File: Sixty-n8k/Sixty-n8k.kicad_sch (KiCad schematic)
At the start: 65 parts, among them J1 USB4085-GF-A_REVB, J2 SD_CARD_PORT, J3 Conn_02x32_Odd_Even, J4 Conn_01x02, SW1 RESET, SW2 DEBUG, U1 74LS05, U10 74HC164, U11 74LS393, U13 74LS148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

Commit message: Starting to hand route. want to just layout and see what autorouter does though...
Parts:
- D1: value LED_ALT -> POWER; symbol n8-bit-special-rescue:LED_ALT-Device -> Device:LED
- D2: value LED_ALT -> HALT; symbol n8-bit-special-rescue:LED_ALT-Device -> Device:LED
- D3: value LED_ALT -> RX; symbol n8-bit-special-rescue:LED_ALT-Device -> Device:LED
- D4: value LED_ALT -> TX; symbol n8-bit-special-rescue:LED_ALT-Device -> Device:LED
- J2: footprint Connector_PinHeader_2.54mm:PinHeader_2x08_P2.54mm_Vertical -> Connector_PinSocket_2.54mm:PinSocket_2x08_P2.54mm_Vertical
- J4: footprint Connector_PinSocket_2.54mm:PinSocket_1x02_P2.54mm_Vertical -> Connector_PinHeader_2.54mm:PinHeader_1x02_P2.54mm_Vertical
- U3: value AM29F040B-70J -> ODD_ROM
- U4: value AS6C4008-55PCN -> ODD_RAM
- U7: value AS6C4008-55PCN -> EVEN_RAM
- U8: value AM29F040B-70J -> EVEN_ROM
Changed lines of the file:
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@@
       (effects (font (size 1.27 1.27)) (justify left))
     )
-    (property "Value" "AS6C4008-55PCN" (at 342.3159 30.099 0)
+    (property "Value" "ODD_RAM" (at 342.3159 30.099 0)
       (effects (font (size 1.27 1.27)) (justify left))
     )
@@
     )
   )
-  (symbol (lib_id "n8-bit-special-rescue:LED_ALT-Device") (at 558.8 300.99 90) (unit 1)
+  (symbol (lib_id "Device:LED") (at 558.8 300.99 90) (unit 1)
     (in_bom yes) (on_board yes) (dnp no)
     (property "Reference" "D4" (at 553.2882 301.1678 0)
       (effects (font (size 1.27 1.27)))
     )
-    (property "Value" "LED_ALT" (at 555.5996 301.1678 0)
+    (property "Value" "TX" (at 555.5996 301.1678 0)
       (effects (font (size 1.27 1.27)))
     )
@@
       (effects (font (size 1.27 1.27)))
     )
-    (property "Footprint" "Connector_PinHeader_2.54mm:PinHeader_2x08_P2.54mm_Vertical" (at 530.86 207.01 0)
+    (property "Footprint" "Connector_PinSocket_2.54mm:PinSocket_2x08_P2.54mm_Vertical" (at 530.86 207.01 0)
       (effects (font (size 1.27 1.27)) hide)
     )
@@
     )
   )
-  (symbol (lib_id "n8-bit-special-rescue:LED_ALT-Device") (at 548.64 300.99 90) (unit 1)
+  (symbol (lib_id "Device:LED") (at 548.64 300.99 90) (unit 1)
     (in_bom yes) (on_board yes) (dnp no)
     (property "Reference" "D3" (at 543.1282 301.1678 0)
       (effects (font (size 1.27 1.27)))
     )
-    (property "Value" "LED_ALT" (at 545.4396 301.1678 0)
+    (property "Value" "RX" (at 545.4396 301.1678 0)
       (effects (font (size 1.27 1.27)))
     )
@@
     )
   )
-  (symbol (lib_id "n8-bit-special-rescue:LED_ALT-Device") (at 118.11 91.44 0) (unit 1)
+  (symbol (lib_id "Device:LED") (at 118.11 91.44 0) (unit 1)
     (in_bom yes) (on_board yes) (dnp no)
     (property "Reference" "D2" (at 117.9322 85.9282 0)
       (effects (font (size 1.27 1.27)))
     )
-    (property "Value" "LED_ALT" (at 117.9322 88.2396 0)
+    (property "Value" "HALT" (at 117.9322 88.2396 0)
       (effects (font (size 1.27 1.27)))
     )
@@
       (effects (font (size 1.27 1.27)) (justify left))
     )
-    (property "Value" "AM29F040B-70J" (at 433.7559 96.774 0)
+    (property "Value" "EVEN_ROM" (at 433.7559 96.774 0)
       (effects (font (size 1.27 1.27)) (justify left))
     )
@@
       (effects (font (size 1.27 1.27)) (justify left))
     )
-    (property "Value" "AM29F040B-70J" (at 433.7559 30.734 0)
+    (property "Value" "ODD_ROM" (at 433.7559 30.734 0)
       (effects (font (size 1.27 1.27)) (justify left))
     )
@@
     )
   )
-  (symbol (lib_id "n8-bit-special-rescue:LED_ALT-Device") (at 118.11 71.12 0) (unit 1)
+  (symbol (lib_id "Device:LED") (at 118.11 71.12 0) (unit 1)
     (in_bom yes) (on_board yes) (dnp no)
     (property "Reference" "D1" (at 117.9322 65.6082 0)
       (effects (font (size 1.27 1.27)))
     )
-    (property "Value" "LED_ALT" (at 117.9322 67.9196 0)
+    (property "Value" "POWER" (at 117.9322 67.9196 0)
       (effects (font (size 1.27 1.27)))
     )
@@
       (effects (font (size 1.27 1.27)) (justify left))
     )
-    (property "Footprint" "Connector_PinSocket_2.54mm:PinSocket_1x02_P2.54mm_Vertical" (at 314.325 216.535 0)
+    (property "Footprint" "Connector_PinHeader_2.54mm:PinHeader_1x02_P2.54mm_Vertical" (at 314.325 216.535 0)
       (effects (font (size 1.27 1.27)) hide)
     )
@@
       (effects (font (size 1.27 1.27)) (justify left))
     )
-    (property "Value" "AS6C4008-55PCN" (at 342.3159 96.139 0)
+    (property "Value" "EVEN_RAM" (at 342.3159 96.139 0)
       (effects (font (size 1.27 1.27)) (justify left))
     )

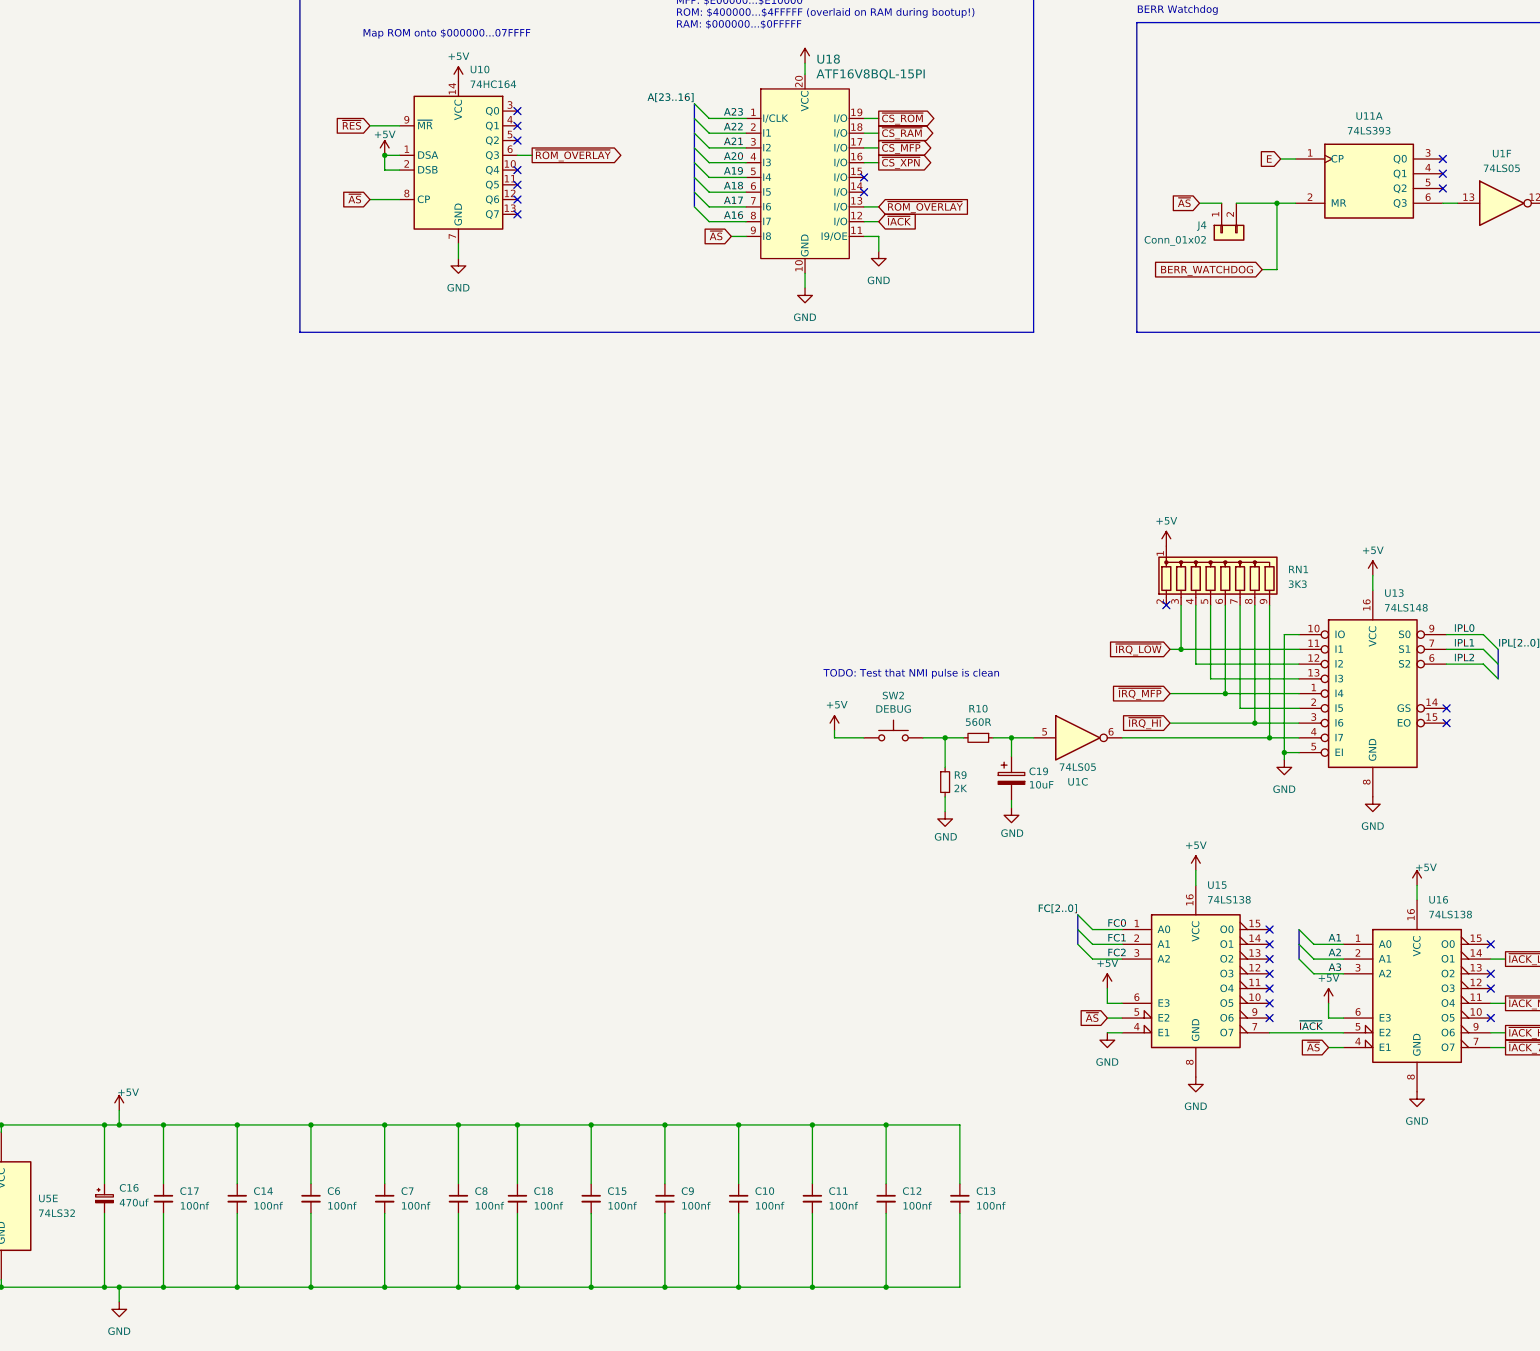
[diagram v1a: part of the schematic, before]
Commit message: new layout, start of hand routing but very complex
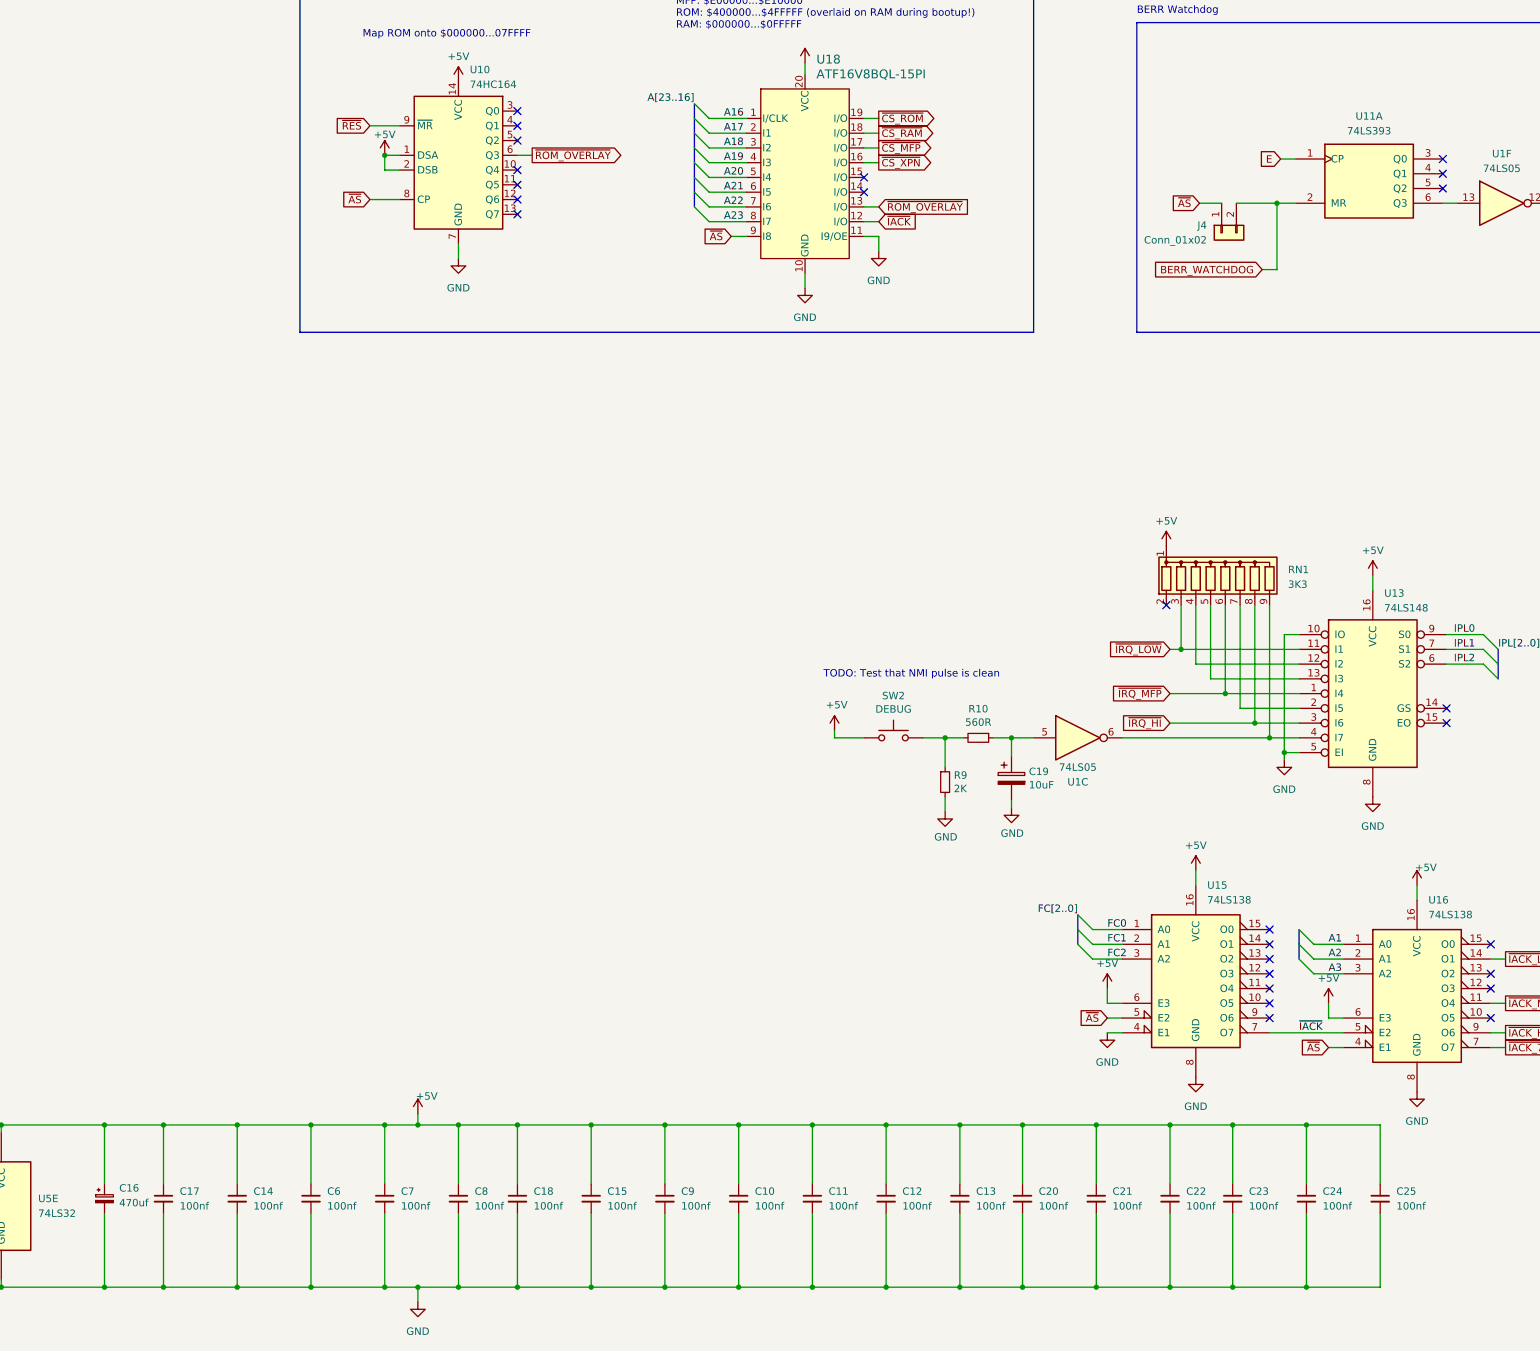
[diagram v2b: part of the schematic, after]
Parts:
- added C20, C21, C22, C23, C24, C25: 100nf, Capacitor_THT:C_Disc_D5.0mm_W2.5mm_P2.50mm, symbol Device:C_Small
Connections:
- net +5V: now also C20.1, C21.1, C22.1, C23.1, C24.1, C25.1
- net A16: now also U18.1 (I/CLK); no longer U18.8 (I7)
- net A17: now also U18.2 (I1); no longer U18.7 (I6)
- net A18: now also U18.3 (I2); no longer U18.6 (I5)
- net A19: now also U18.4 (I3); no longer U18.5 (I4)
- net A20: now also U18.5 (I4); no longer U18.4 (I3)
- net A21: now also U18.6 (I5); no longer U18.3 (I2)
- net A22: now also U18.7 (I6); no longer U18.2 (I1)
- net A23: now also U18.8 (I7); no longer U18.1 (I/CLK)
- net GND: now also C20.2, C21.2, C22.2, C23.2, C24.2, C25.2

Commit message: Autoroute success (don't judge me)
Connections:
- net A1: now also J3.31 (Pin_31); no longer J3.5 (Pin_5)
- net A10: now also J3.49 (Pin_49); no longer J3.23 (Pin_23)
- net A11: now also J3.51 (Pin_51); no longer J3.25 (Pin_25)
- net A12: now also J3.53 (Pin_53); no longer J3.27 (Pin_27)
- net A13: now also J3.55 (Pin_55); no longer J3.29 (Pin_29)
- net A14: now also J3.57 (Pin_57); no longer J3.31 (Pin_31)
- net A15: now also J3.59 (Pin_59); no longer J3.33 (Pin_33)
- net A2: now also J3.33 (Pin_33); no longer J3.7 (Pin_7)
- net A3: now also J3.35 (Pin_35); no longer J3.9 (Pin_9)
- net A4: now also J3.37 (Pin_37); no longer J3.11 (Pin_11)
- net A5: now also J3.39 (Pin_39); no longer J3.13 (Pin_13)
- net A6: now also J3.41 (Pin_41); no longer J3.15 (Pin_15)
- net A7: now also J3.43 (Pin_43); no longer J3.17 (Pin_17)
- net A8: now also J3.45 (Pin_45); no longer J3.19 (Pin_19)
- net A9: now also J3.47 (Pin_47); no longer J3.21 (Pin_21)
- net CLK_{CPU}: now also J3.29 (Pin_29); no longer J3.59 (Pin_59)
- net CLK_{HALF}: now also J3.18 (Pin_18); no longer J3.60 (Pin_60)
- net D0: now also J3.60 (Pin_60); no longer J3.6 (Pin_6)
- net D1: now also J3.58 (Pin_58); no longer J3.8 (Pin_8)
- net D10: now also J3.40 (Pin_40); no longer J3.26 (Pin_26)
- net D11: now also J3.38 (Pin_38); no longer J3.28 (Pin_28)
- net D12: now also J3.36 (Pin_36); no longer J3.30 (Pin_30)
- net D13: now also J3.34 (Pin_34); no longer J3.32 (Pin_32)
- net D14: now also J3.32 (Pin_32); no longer J3.34 (Pin_34)
- net D15: now also J3.30 (Pin_30); no longer J3.36 (Pin_36)
- net D2: now also J3.56 (Pin_56); no longer J3.10 (Pin_10)
- net D3: now also J3.54 (Pin_54); no longer J3.12 (Pin_12)
- net D4: now also J3.52 (Pin_52); no longer J3.14 (Pin_14)
- net D5: now also J3.50 (Pin_50); no longer J3.16 (Pin_16)
- net D6: now also J3.48 (Pin_48); no longer J3.18 (Pin_18)
- net D7: now also J3.46 (Pin_46); no longer J3.20 (Pin_20)
- net D8: now also J3.44 (Pin_44); no longer J3.22 (Pin_22)
- net D9: now also J3.42 (Pin_42); no longer J3.24 (Pin_24)
- net E: now also J3.21 (Pin_21); no longer J3.51 (Pin_51)
- net R~{W}: now also J3.9 (Pin_9); no longer J3.39 (Pin_39)
- net ~{AS}: now also J3.11 (Pin_11); no longer J3.41 (Pin_41)
- net ~{BERR}: now also J3.12 (Pin_12); no longer J3.54 (Pin_54)
- net ~{BGACK}: now also J3.28 (Pin_28), RN3.3 (R2); no longer J3.46 (Pin_46), RN2.9 (R8)
- net ~{BG}: now also J3.8 (Pin_8); no longer J3.50 (Pin_50)
- net ~{BR}: now also J3.10 (Pin_10), RN3.2 (R1); no longer J3.52 (Pin_52), RN2.8 (R7)
- net ~{CS_XPN}: now also J3.15 (Pin_15); no longer J3.45 (Pin_45)
- net ~{DTACK_MFP}: now also RN2.8 (R7); no longer RN3.2 (R1)
- net ~{DTACK_XPN}: now also J3.13 (Pin_13), RN2.9 (R8); no longer J3.43 (Pin_43), RN3.3 (R2)
- net ~{IACK_HI}: now also J3.26 (Pin_26); no longer J3.44 (Pin_44)
- net ~{IACK_LOW}: now also J3.24 (Pin_24); no longer J3.42 (Pin_42)
- net ~{IRQ_HI}: now also J3.22 (Pin_22), RN1.3 (R2); no longer J3.40 (Pin_40), RN1.8 (R7)
- net ~{IRQ_LOW}: now also J3.20 (Pin_20), RN1.8 (R7); no longer J3.38 (Pin_38), RN1.3 (R2)
- net ~{IRQ_MFP}: now also RN1.5 (R4); no longer RN1.6 (R5)
- net ~{LDS}: now also J3.5 (Pin_5), RN3.7 (R6); no longer J3.35 (Pin_35), RN3.8 (R7)
- net ~{RES}: now also J3.27 (Pin_27); no longer J3.57 (Pin_57)
- net ~{UDS}: now also J3.7 (Pin_7), RN3.8 (R7); no longer J3.37 (Pin_37), RN3.7 (R6)
- net ~{VMA}: now also J3.19 (Pin_19); no longer J3.49 (Pin_49)
- net ~{VPA}: now also J3.23 (Pin_23); no longer J3.53 (Pin_53)
- net at U13.12 (I2): now also RN1.7 (R6); no longer RN1.4 (R3)
- net at U13.13 (I3): now also RN1.6 (R5); no longer RN1.5 (R4)
- net at U13.2 (I5): now also RN1.4 (R3); no longer RN1.7 (R6)
- net at U1.6, U13.4 (I7): now also RN1.2 (R1); no longer RN1.9 (R8)

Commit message: About to remove 2nd 74HC138
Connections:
- net A1: now also J3.59 (Pin_59); no longer J3.31 (Pin_31)
- net A10: now also J3.41 (Pin_41); no longer J3.49 (Pin_49)
- net A11: now also J3.39 (Pin_39); no longer J3.51 (Pin_51)
- net A12: now also J3.37 (Pin_37); no longer J3.53 (Pin_53)
- net A13: now also J3.35 (Pin_35); no longer J3.55 (Pin_55)
- net A14: now also J3.33 (Pin_33); no longer J3.57 (Pin_57)
- net A15: now also J3.31 (Pin_31); no longer J3.59 (Pin_59)
- net A2: now also J3.57 (Pin_57); no longer J3.33 (Pin_33)
- net A3: now also J3.55 (Pin_55); no longer J3.35 (Pin_35)
- net A4: now also J3.53 (Pin_53); no longer J3.37 (Pin_37)
- net A5: now also J3.51 (Pin_51); no longer J3.39 (Pin_39)
- net A6: now also J3.49 (Pin_49); no longer J3.41 (Pin_41)
- net A7: now also J3.47 (Pin_47); no longer J3.43 (Pin_43)
- net A9: now also J3.43 (Pin_43); no longer J3.47 (Pin_47)
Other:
- note added: "Interrupt Generation and Handling"
- moved on the sheet: C19, C4, C5, D3, D4, J2, J4, R10, R7, R8, R9, RN1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
